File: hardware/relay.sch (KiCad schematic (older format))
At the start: 13 parts, among them J11 LOAD, K11 SRD-05VDC-SL-C, Q11 PMBT3904, U31 PC817X2CSP9F, U32 CC6902SO-10A

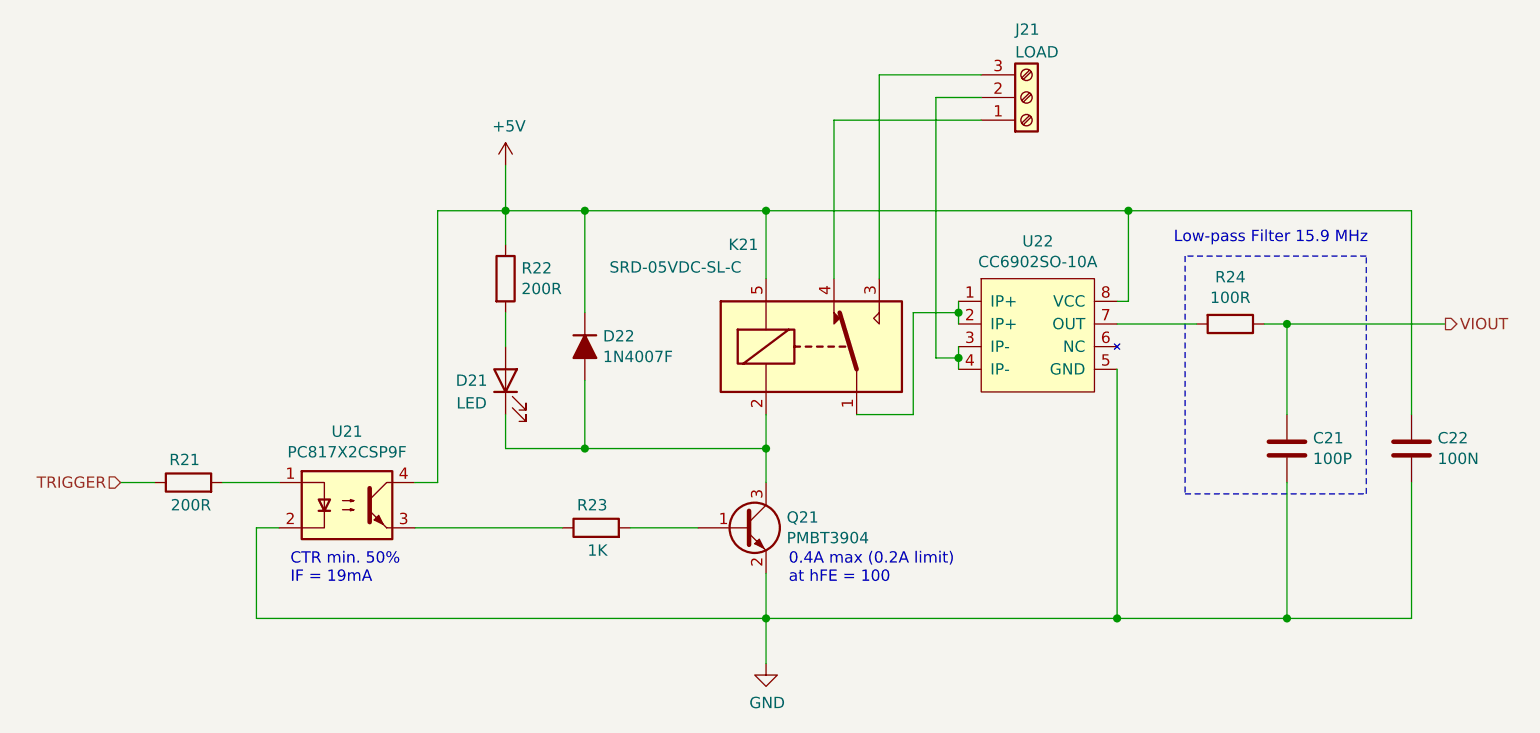
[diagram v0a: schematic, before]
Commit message: traces done
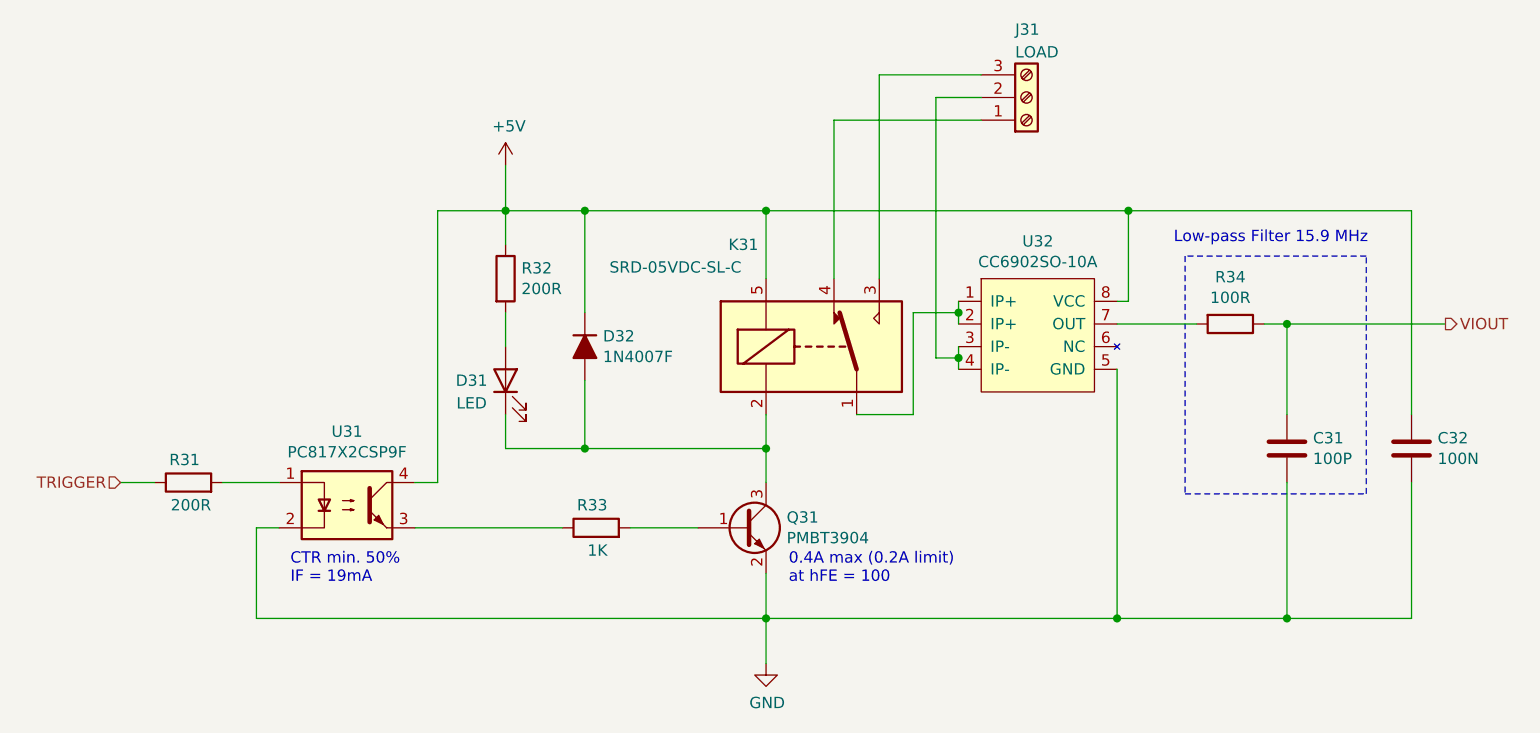
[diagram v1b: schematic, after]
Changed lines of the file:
@@
 $Descr A4 11693 8268
 encoding utf-8
-Sheet 5 5
+Sheet 3 5
 Title "Relay Subsystem"
 Date "2021-06-11"
@@
 AR Path="/60CBD77D/60C3AACC" Ref="Q31"  Part="1"
 AR Path="/60CBD7BB/60C3AACC" Ref="Q41"  Part="1"
-F 0 "Q21" H 5541 4296 50  0000 L CNN
+F 0 "Q31" H 5541 4296 50  0000 L CNN
 F 1 "PMBT3904" H 5541 4205 50  0000 L CNN
 F 2 "Package_TO_SOT_SMD:SOT-23" H 5550 4350 50  0001 C CNN
@@
 AR Path="/60CBD77D/60C3DB9C" Ref="R33"  Part="1"
 AR Path="/60CBD7BB/60C3DB9C" Ref="R43"  Part="1"
-F 0 "R23" V 4800 4200 50  0000 L CNN
+F 0 "R33" V 4800 4200 50  0000 L CNN
 F 1 "1K" V 4600 4200 50  0000 L CNN
 F 2 "Resistor_SMD:R_0805_2012Metric" V 4630 4250 50  0001 C CNN
@@
 AR Path="/60CBD77D/60C4BBD2" Ref="J31"  Part="1"
 AR Path="/60CBD7BB/60C4BBD2" Ref="J41"  Part="1"
-F 0 "J21" H 6550 2050 50  0000 L CNN
+F 0 "J31" H 6550 2050 50  0000 L CNN
 F 1 "LOAD" H 6550 2150 50  0000 L CNN
 F 2 "TerminalBlock_Phoenix:TerminalBlock_Phoenix_MKDS-1,5-3_1x03_P5.00mm_Horizontal" H 6600 2350 50  0001 C CNN
@@
 AR Path="/60CBD77D/60C370D4" Ref="K31"  Part="1"
 AR Path="/60CBD7BB/60C370D4" Ref="K41"  Part="1"
-F 0 "K21" H 5350 3900 50  0000 C CNN
+F 0 "K31" H 5350 3900 50  0000 C CNN
 F 1 "SRD-05VDC-SL-C" H 5050 3800 50  0000 C CNN
 F 2 "Relay_THT:Relay_SPDT_SANYOU_SRD_Series_Form_C" H 6100 3400 50  0001 L CNN
@@
 AR Path="/60CBD77D/60C91E1E" Ref="#PWR032"  Part="1"
 AR Path="/60CBD7BB/60C91E1E" Ref="#PWR042"  Part="1"
-F 0 "#PWR022" H 5450 4600 50  0001 C CNN
+F 0 "#PWR032" H 5450 4600 50  0001 C CNN
 F 1 "GND" H 5455 4677 50  0000 C CNN
 F 2 "" H 5450 4850 50  0001 C CNN
@@
 AR Path="/60CBD6BF/60D16B35" Ref="U22"  Part="1"
 AR Path="/60CBD7BB/60D16B35" Ref="U42"  Part="1"
-F 0 "U22" H 6650 3815 50  0000 C CNN
+F 0 "U32" H 6650 3815 50  0000 C CNN
 F 1 "CC6902SO-10A" H 6650 3724 50  0000 C CNN
 F 2 "CustomComponents:CC690XSO-XA" H 6650 3100 50  0001 C CNN
@@
 AR Path="/60CBD77D/60CD3C14" Ref="#PWR031"  Part="1"
 AR Path="/60CBD7BB/60CD3C14" Ref="#PWR041"  Part="1"
-F 0 "#PWR021" H 4300 2500 50  0001 C CNN
+F 0 "#PWR031" H 4300 2500 50  0001 C CNN
 F 1 "+5V" H 4315 2823 50  0000 C CNN
 F 2 "" H 4300 2650 50  0001 C CNN
@@
 AR Path="/60CBD77D/60C94FE5" Ref="C31"  Part="1"
 AR Path="/60CBD7BB/60C94FE5" Ref="C41"  Part="1"
-F 0 "C21" H 7865 3946 50  0000 L CNN
+F 0 "C31" H 7865 3946 50  0000 L CNN
 F 1 "100P" H 7865 3855 50  0000 L CNN
 F 2 "Capacitor_SMD:C_0805_2012Metric" H 7788 3750 50  0001 C CNN
@@
 AR Path="/60CBD77D/60CDBA1D" Ref="R34"  Part="1"
 AR Path="/60CBD7BB/60CDBA1D" Ref="R44"  Part="1"
-F 0 "R24" V 7293 3350 50  0000 C CNN
+F 0 "R34" V 7293 3350 50  0000 C CNN
 F 1 "100R" V 7384 3350 50  0000 C CNN
 F 2 "Resistor_SMD:R_0805_2012Metric" V 7430 3350 50  0001 C CNN
@@
 AR Path="/60CBD77D/60C99EC6" Ref="C32"  Part="1"
 AR Path="/60CBD7BB/60C99EC6" Ref="C42"  Part="1"
-F 0 "C22" H 8415 3946 50  0000 L CNN
+F 0 "C32" H 8415 3946 50  0000 L CNN
 F 1 "100N" H 8415 3855 50  0000 L CNN
 F 2 "Capacitor_SMD:C_0805_2012Metric" H 8338 3750 50  0001 C CNN
@@
 AR Path="/60CBD77D/60C3D896" Ref="R32"  Part="1"
 AR Path="/60CBD7BB/60C3D896" Ref="R42"  Part="1"
-F 0 "R22" H 4370 3196 50  0000 L CNN
+F 0 "R32" H 4370 3196 50  0000 L CNN
 F 1 "200R" H 4370 3105 50  0000 L CNN
 F 2 "Resistor_SMD:R_0805_2012Metric" V 4230 3150 50  0001 C CNN
@@
 AR Path="/60CBD77D/60C544FE" Ref="D32"  Part="1"
 AR Path="/60CBD7BB/60C544FE" Ref="D42"  Part="1"
-F 0 "D22" V 4604 3530 50  0000 L CNN
+F 0 "D32" V 4604 3530 50  0000 L CNN
 F 1 "1N4007F" V 4695 3530 50  0000 L CNN
 F 2 "Diode_SMD:D_SMA" H 4650 3450 50  0001 C CNN
@@
 AR Path="/60CBD77D/60C3C98C" Ref="D31"  Part="1"
 AR Path="/60CBD7BB/60C3C98C" Ref="D41"  Part="1"
-F 0 "D21" V 4300 3750 50  0000 C CNN
+F 0 "D31" V 4300 3750 50  0000 C CNN
 F 1 "LED" V 4200 3750 50  0000 C CNN
 F 2 "LED_SMD:LED_0805_2012Metric" H 4300 3600 50  0001 C CNN
@@
 AR Path="/60CBD6BF/60D16537" Ref="U21"  Part="1"
 AR Path="/60CBD7BB/60D16537" Ref="U41"  Part="1"
-F 0 "U21" H 3600 4475 50  0000 C CNN
+F 0 "U31" H 3600 4475 50  0000 C CNN
 F 1 "PC817X2CSP9F" H 3600 4384 50  0000 C CNN
 F 2 "CustomComponents:PC817X2CSP9F" H 3400 3950 50  0001 L CIN
@@
 AR Path="/60CBD77D/60C3E090" Ref="R31"  Part="1"
 AR Path="/60CBD7BB/60C3E090" Ref="R41"  Part="1"
-F 0 "R21" V 3000 4000 50  0000 L CNN
+F 0 "R31" V 3000 4000 50  0000 L CNN
 F 1 "200R" V 2800 3950 50  0000 L CNN
 F 2 "Resistor_SMD:R_0805_2012Metric" V 2830 4050 50  0001 C CNN
